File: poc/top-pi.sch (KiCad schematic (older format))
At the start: 108 parts

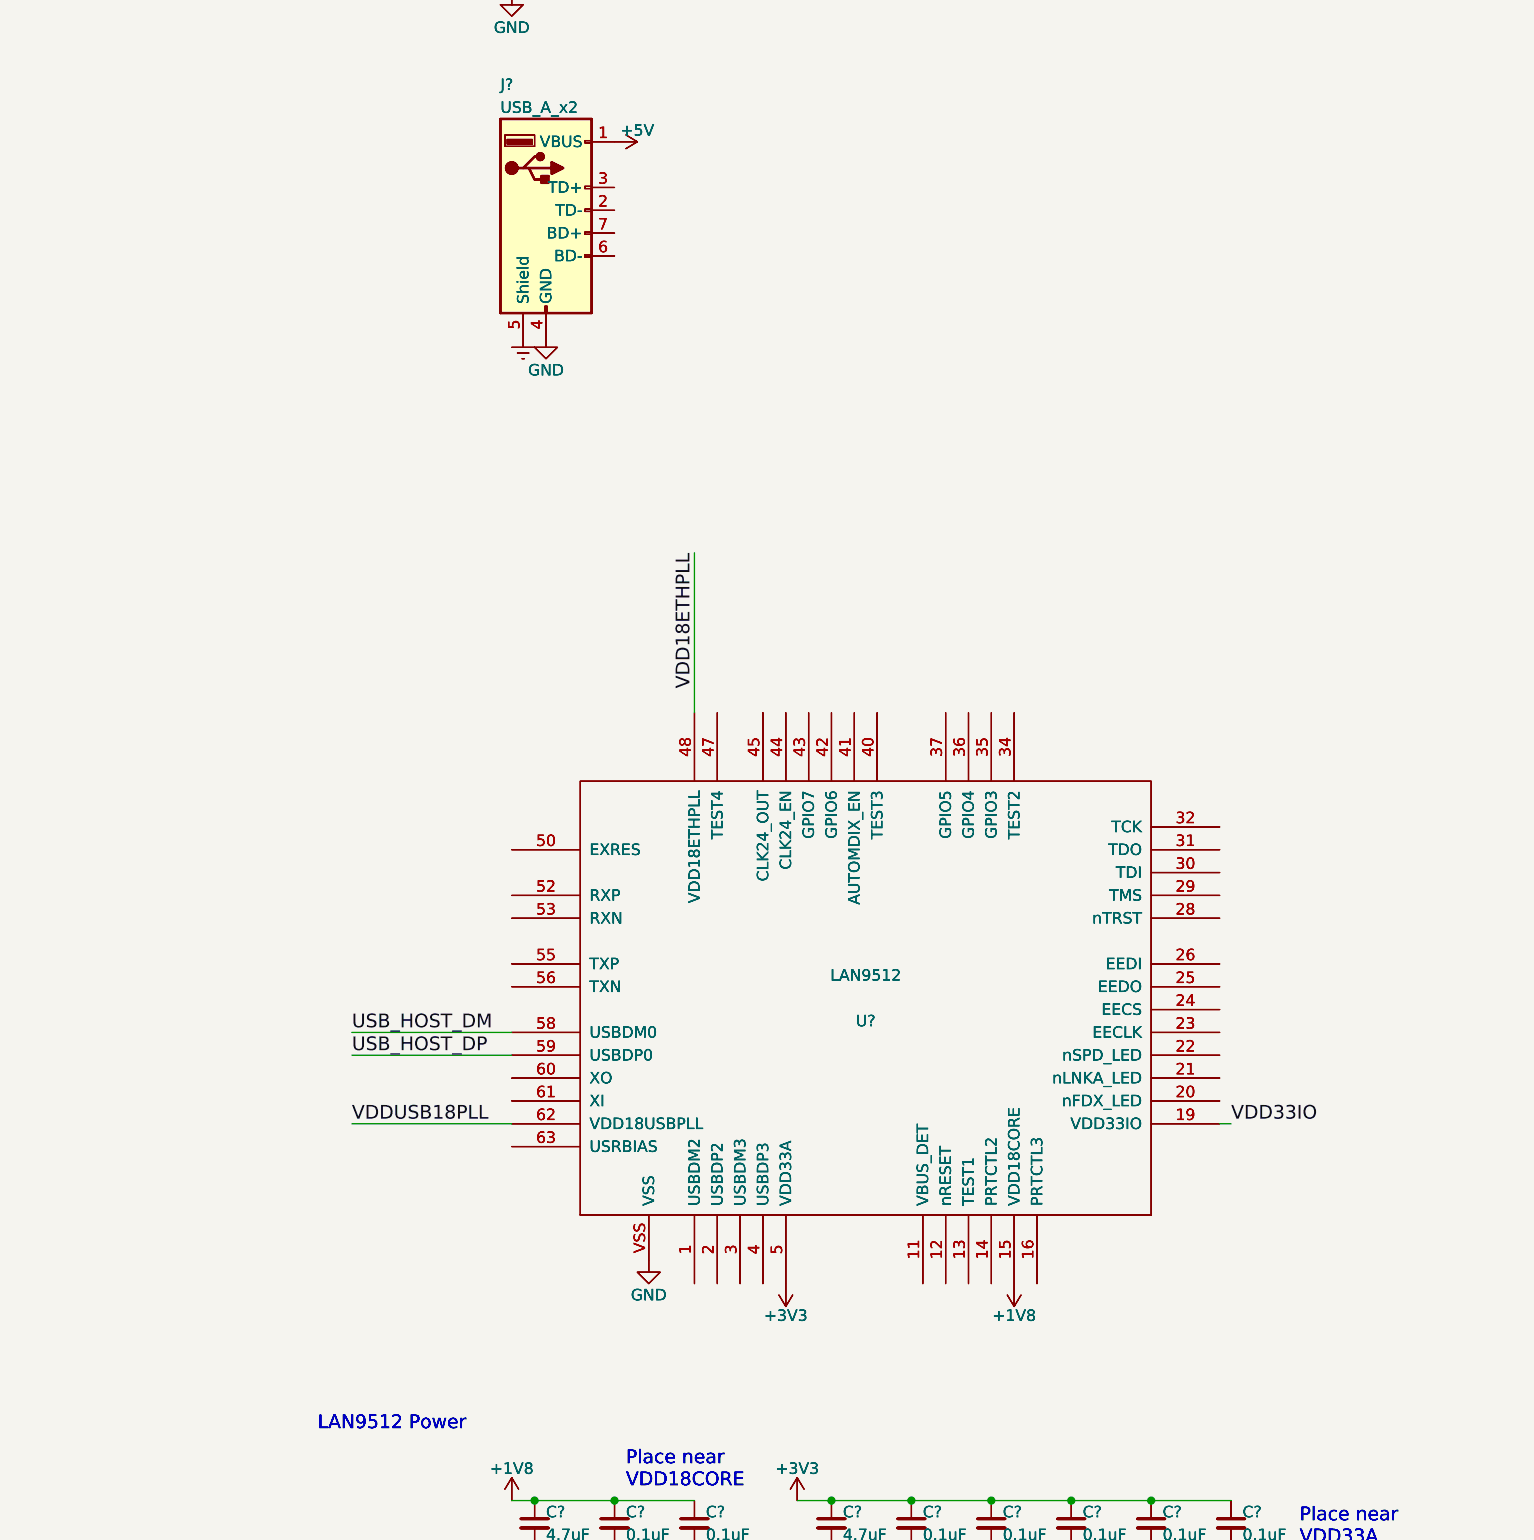
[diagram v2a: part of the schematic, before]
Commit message: Finish LAN9512 USB layout
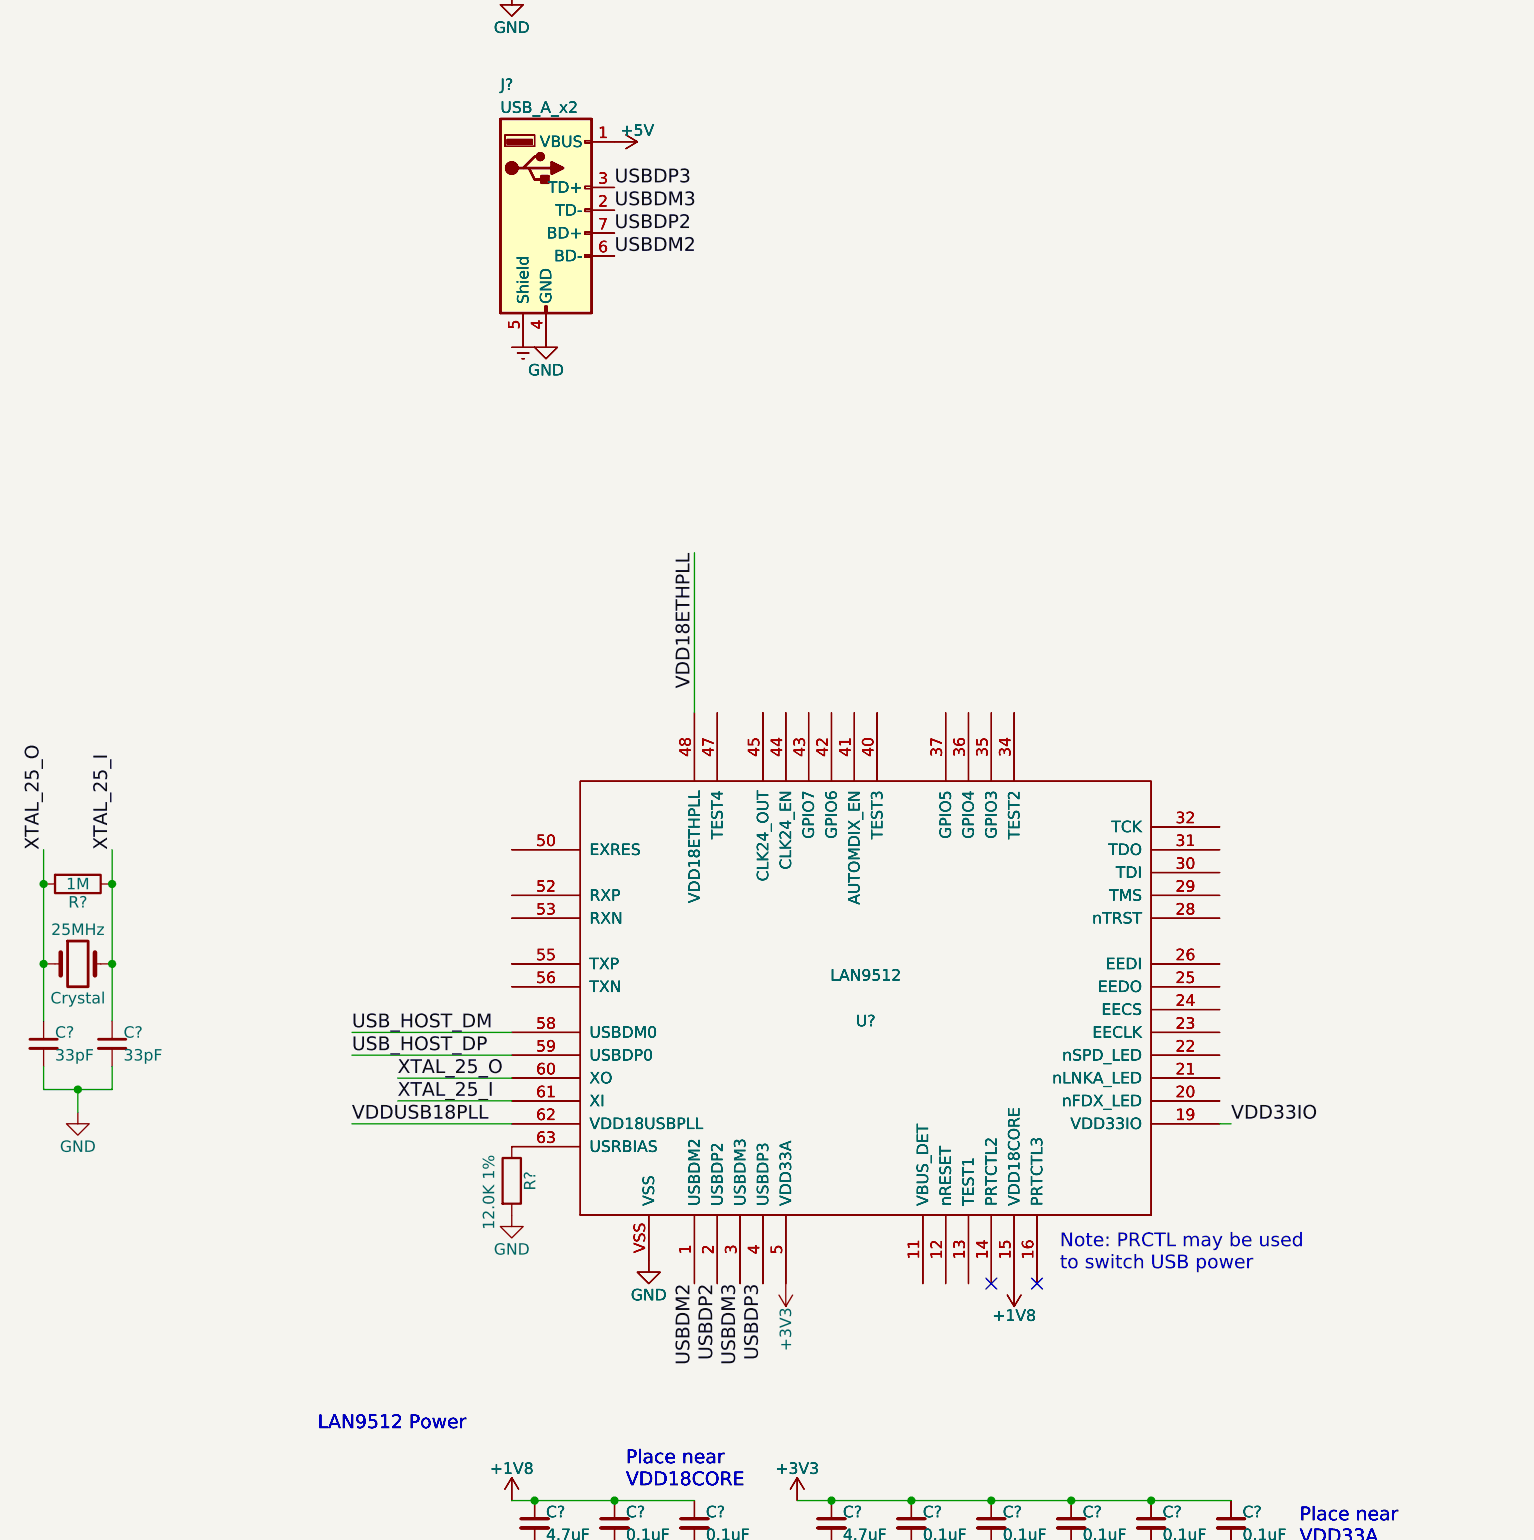
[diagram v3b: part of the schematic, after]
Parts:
- added 25MHz: Crystal, symbol Crystal
- added C? (x2): 33pF, symbol C_Small
- added R?: 12.0K 1%, symbol R
- added R?: 1M, symbol R
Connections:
- net GND: now also C?.2, C?.2, R?.2
- net USBDM2: now reaches U?.1 (USBDM2), U?.1 (USBDM2)
- net USBDM2: now also J?.6 (BD-), J?.6 (BD-)
- net USBDP2: now reaches U?.2 (USBDP2), U?.2 (USBDP2)
- net USBDP2: now also J?.7 (BD+), J?.7 (BD+)
- net USBDM3: now reaches U?.3 (USBDM3), U?.3 (USBDM3)
- net USBDM3: now also J?.2 (TD-), J?.2 (TD-)
- net USBDP3: now reaches U?.4 (USBDP3), U?.4 (USBDP3)
- net USBDP3: now also J?.3 (TD+), J?.3 (TD+)
- net XTAL_25_O: now reaches U?.60 (XO), U?.60 (XO)
- net XTAL_25_O: now also 25MHz.1, C?.1, R?.2
- net XTAL_25_I: now reaches U?.61 (XI), U?.61 (XI)
- net XTAL_25_I: now also 25MHz.2, C?.1, R?.1
- net at U?.63 (USRBIAS), U?.63 (USRBIAS): now also R?.1
- no-connect marks 0 -> 2
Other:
- note added: "Note: PRCTL may be used\nto switch USB power"

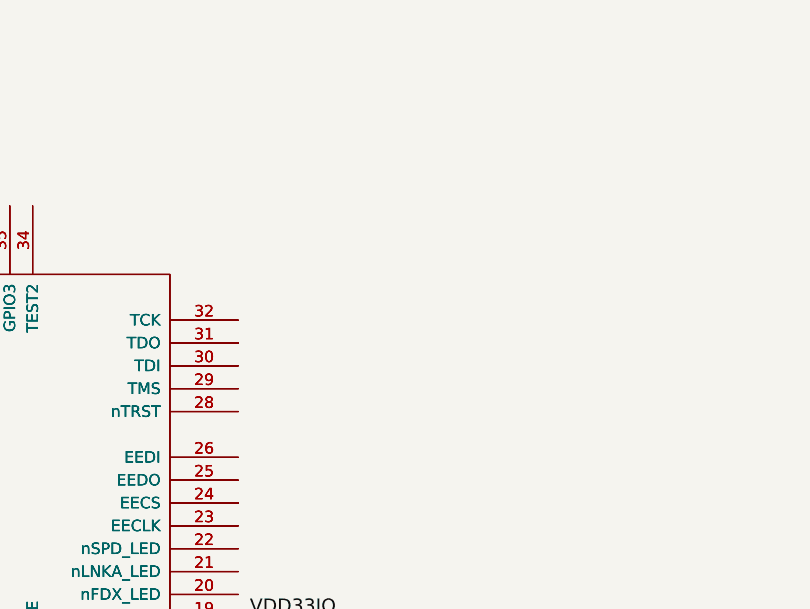
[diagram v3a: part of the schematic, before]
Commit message: LAN9512 JTAG header
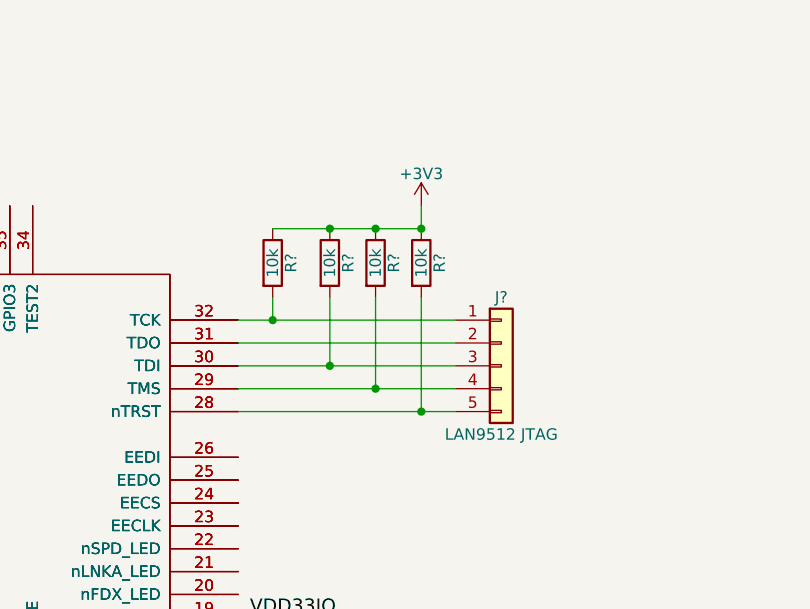
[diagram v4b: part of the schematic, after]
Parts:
- added J?: LAN9512 JTAG, symbol Conn_01x05
- added R? (x4): 10k, symbol R
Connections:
- net +3V3: now also R?.1, R?.1, R?.1, R?.1
- net at U?.28 (nTRST), U?.28 (nTRST): now also J?.5 (Pin_5), R?.2
- net at U?.29 (TMS), U?.29 (TMS): now also J?.4 (Pin_4), R?.2
- net at U?.30 (TDI), U?.30 (TDI): now also J?.3 (Pin_3), R?.2
- net at U?.31 (TDO), U?.31 (TDO): now also J?.2 (Pin_2)
- net at U?.32 (TCK), U?.32 (TCK): now also J?.1 (Pin_1), R?.2
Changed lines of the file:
@@
 Connection ~ 900  11900
 Connection ~ 900  12250
+$Comp
+L Conn_01x05 J?
+U 1 1 5A565AAD
+P 7200 11850
+F 0 "J?" H 7200 12150 50  0000 C CNN
+F 1 "LAN9512 JTAG" H 7200 11550 50  0000 C CNN
+F 2 "" H 7200 11850 50  0001 C CNN
+F 3 "" H 7200 11850 50  0001 C CNN
+	1    7200 11850
+	1    0    0    -1
+$EndComp
+Wire Wire Line
+	6050 11750 7000 11750
+$Comp
+L R R?
+U 1 1 5A566E8D
+P 6200 11400
+F 0 "R?" V 6280 11400 50  0000 C CNN
+F 1 "10k" V 6200 11400 50  0000 C CNN
+F 2 "" V 6130 11400 50  0001 C CNN
+F 3 "" H 6200 11400 50  0001 C CNN
+	1    6200 11400
+	1    0    0    -1
+$EndComp
+$Comp
+L R R?
+U 1 1 5A56736B
+P 6450 11400
+F 0 "R?" V 6530 11400 50  0000 C CNN
+F 1 "10k" V 6450 11400 50  0000 C CNN
+F 2 "" V 6380 11400 50  0001 C CNN
+F 3 "" H 6450 11400 50  0001 C CNN
+	1    6450 11400
+	1    0    0    -1
+$EndComp
+$Comp
+L R R?
+U 1 1 5A5674E5
+P 6650 11400
+F 0 "R?" V 6730 11400 50  0000 C CNN
+F 1 "10k" V 6650 11400 50  0000 C CNN
+F 2 "" V 6580 11400 50  0001 C CNN
+F 3 "" H 6650 11400 50  0001 C CNN
+	1    6650 11400
+	1    0    0    -1
+$EndComp
+$Comp
+L R R?
+U 1 1 5A56765C
+P 6850 11400
+F 0 "R?" V 6930 11400 50  0000 C CNN
+F 1 "10k" V 6850 11400 50  0000 C CNN
+F 2 "" V 6780 11400 50  0001 C CNN
+F 3 "" H 6850 11400 50  0001 C CNN
+	1    6850 11400
+	1    0    0    -1
+$EndComp
+Wire Wire Line
+	6050 11650 7000 11650
+Wire Wire Line
+	6050 11850 7000 11850
+Wire Wire Line
+	6050 11950 7000 11950
+Wire Wire Line
+	6050 12050 7000 12050
+Wire Wire Line
+	6200 11550 6200 11650
+Connection ~ 6200 11650
+Wire Wire Line
+	6450 11550 6450 11850
+Connection ~ 6450 11850
+Wire Wire Line
+	6650 11550 6650 11950
+Connection ~ 6650 11950
+Wire Wire Line
+	6850 11550 6850 12050
+Connection ~ 6850 12050
+Wire Wire Line
+	6200 11250 6850 11250
+Connection ~ 6450 11250
+Connection ~ 6650 11250
+$Comp
+L +3V3 #PWR?
+U 1 1 5A568B3C
+P 6850 11150
+F 0 "#PWR?" H 6850 11000 50  0001 C CNN
+F 1 "+3V3" H 6850 11290 50  0000 C CNN
+F 2 "" H 6850 11150 50  0001 C CNN
+F 3 "" H 6850 11150 50  0001 C CNN
+	1    6850 11150
+	1    0    0    -1
+$EndComp
+Wire Wire Line
+	6850 11250 6850 11150
+Connection ~ 6850 11250
 $EndSCHEMATC
